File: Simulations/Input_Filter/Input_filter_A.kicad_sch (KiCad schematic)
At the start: 18 parts, among them U21 TL072

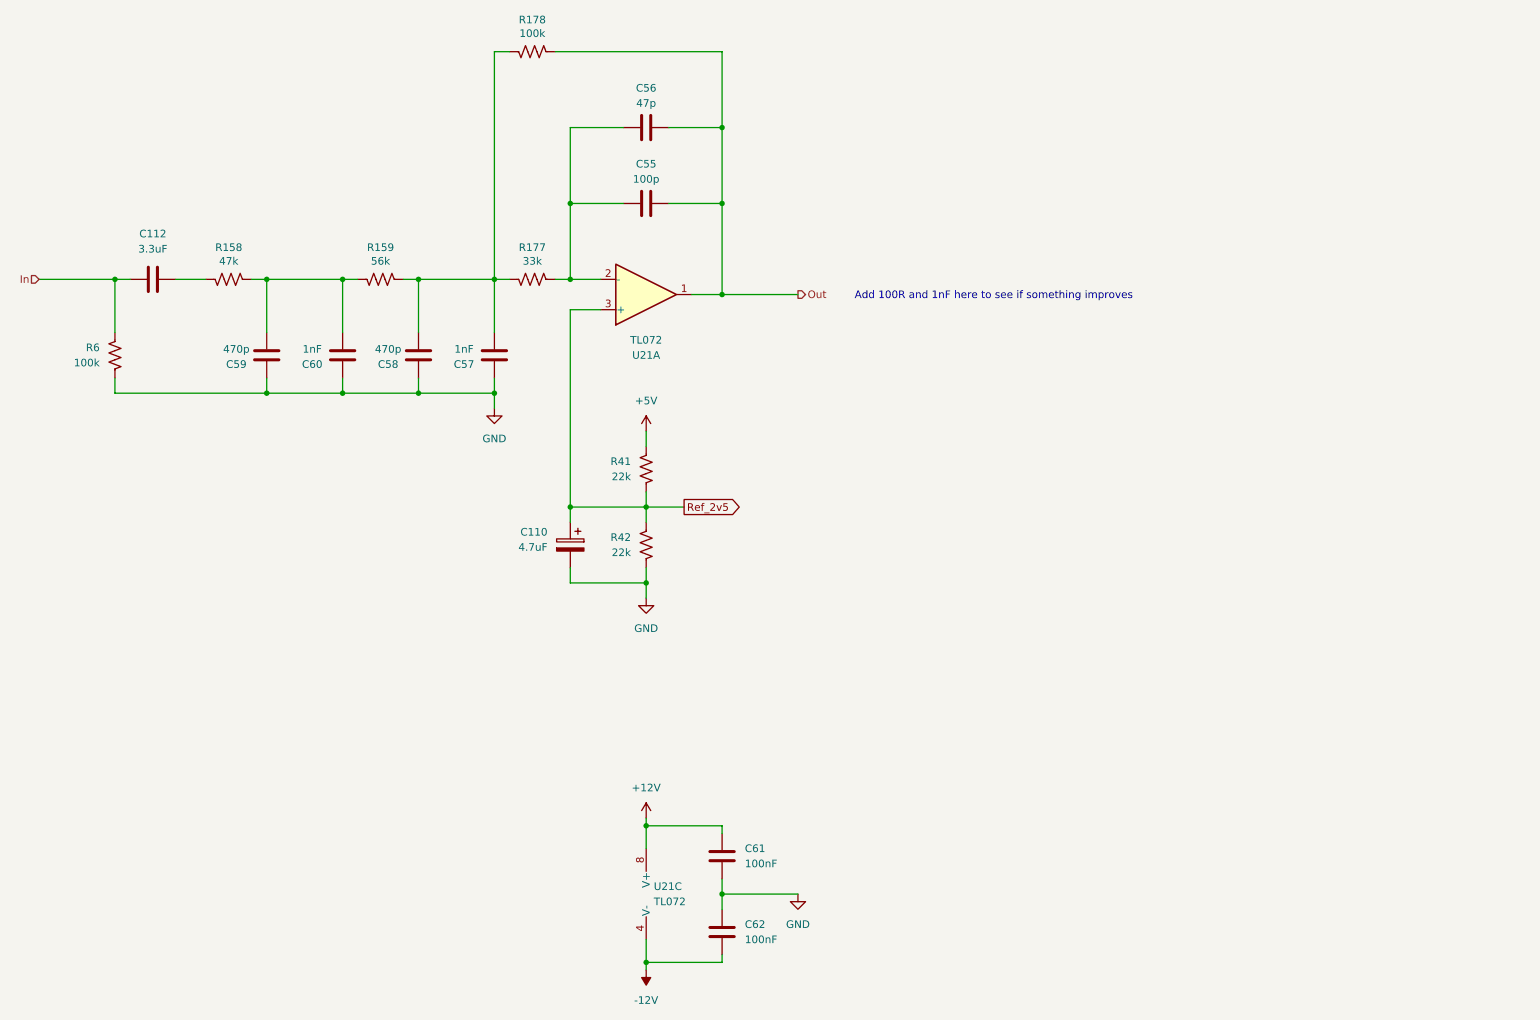
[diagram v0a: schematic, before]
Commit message: Simulated IO filters
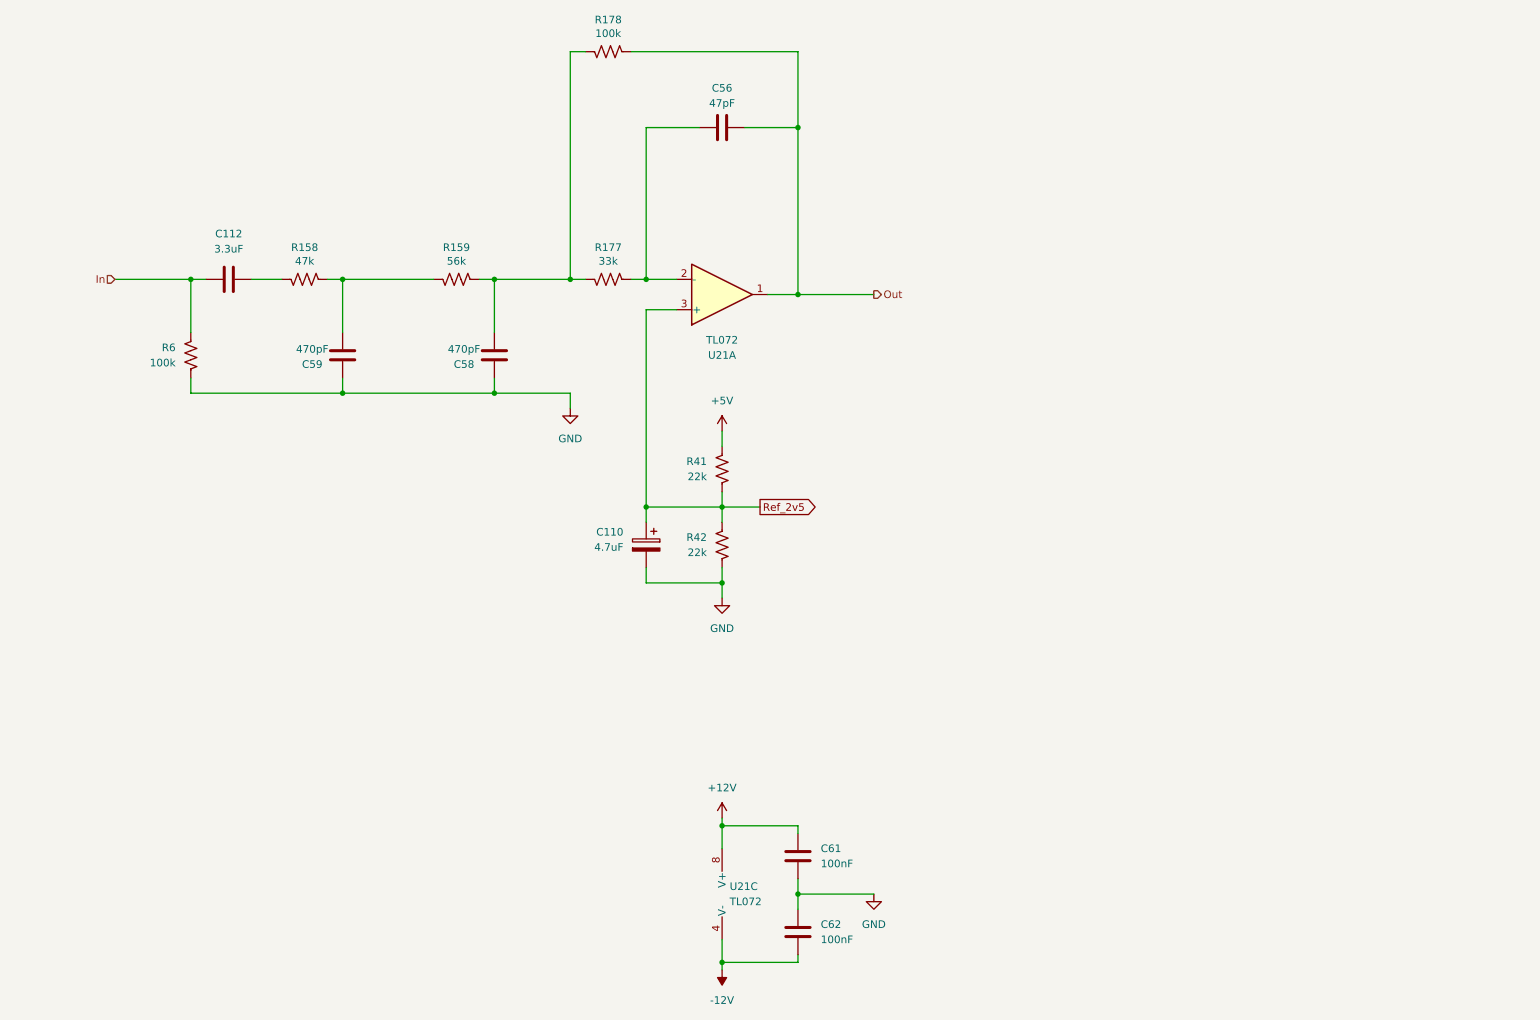
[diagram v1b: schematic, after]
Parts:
- removed C55: 100p, Capacitor_THT:C_Disc_D3.0mm_W2.0mm_P2.50mm, symbol Device:C
- removed C57, C60: 1nF, Capacitor_THT:C_Disc_D3.0mm_W2.0mm_P2.50mm, symbol Device:C
- C56: value 47p -> 47pF
- C58, C59: value 470p -> 470pF
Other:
- note removed: "Add 100R and 1nF here to see if something improves"
- company: DMH Instruments -> (none)

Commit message: Fixed issue with SPICE model
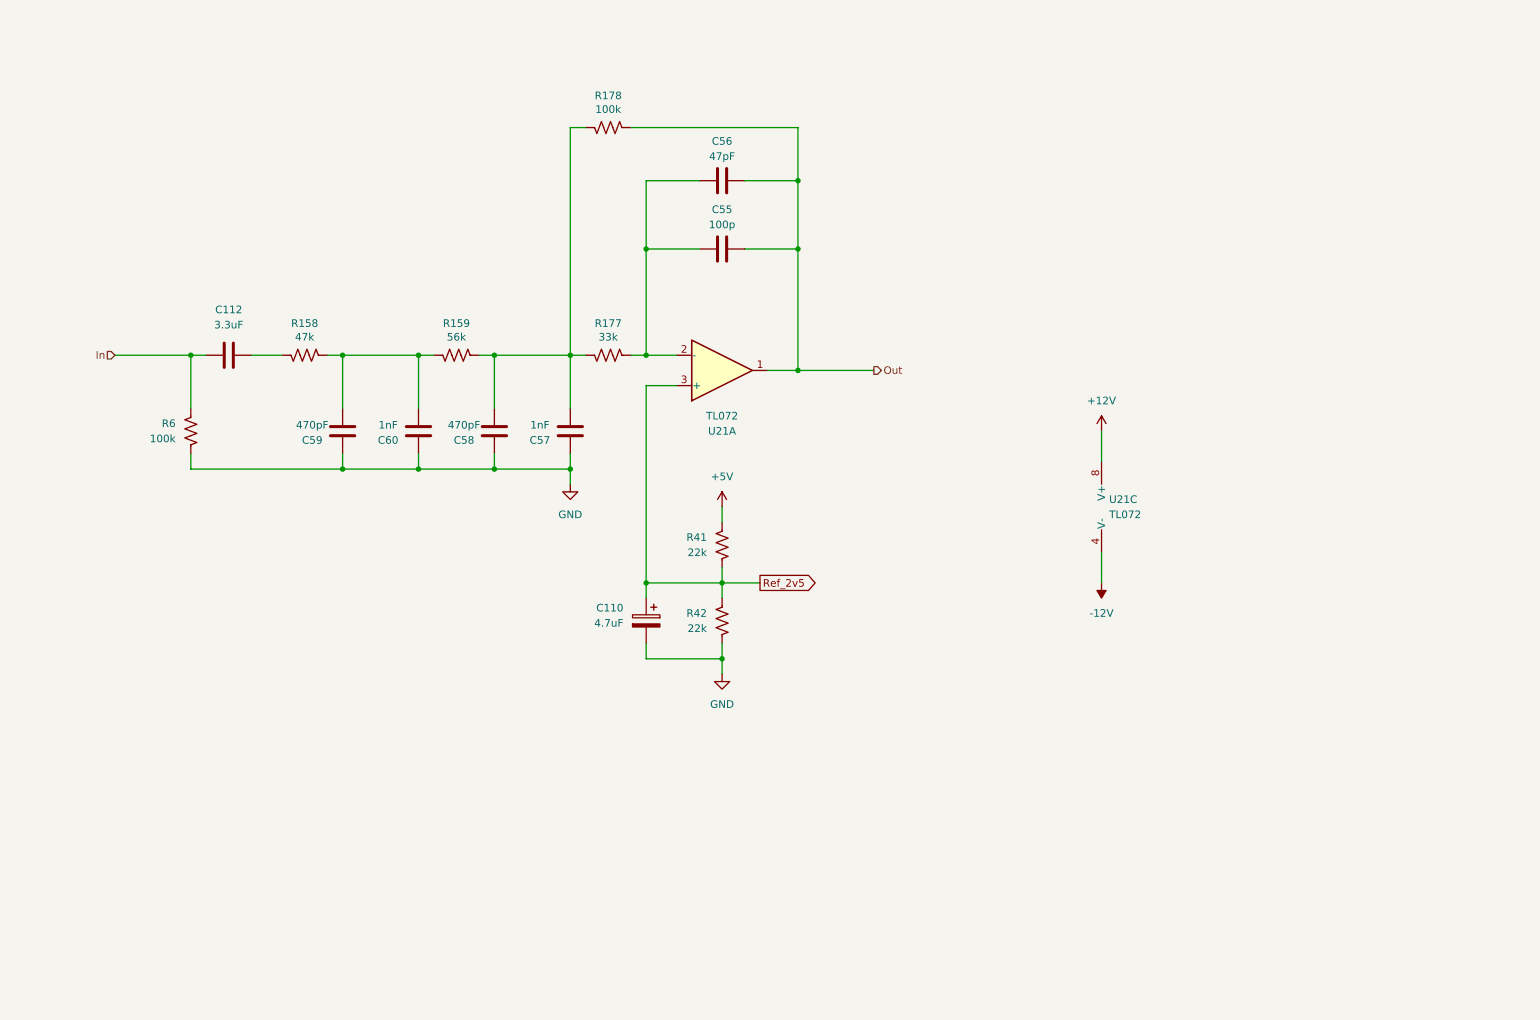
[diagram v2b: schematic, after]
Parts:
- removed C61, C62: 100nF, Capacitor_THT:C_Disc_D4.3mm_W1.9mm_P5.00mm, symbol Device:C
- added C55: 100p, Capacitor_THT:C_Disc_D3.0mm_W2.0mm_P2.50mm, symbol Device:C
- added C57, C60: 1nF, Capacitor_THT:C_Disc_D3.0mm_W2.0mm_P2.50mm, symbol Device:C
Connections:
- net GND: now also C57.1, C60.1
- net Out: now also C55.2
- net at C59.2, R158.2, R159.1: now also C60.2
- net at C58.2, R159.2, R177.1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: now also C57.2
- net at C56.1, R177.2, U21.2 (-): now also C55.1
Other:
- moved on the sheet: C110, C112, C56, C58, C59, R158, R159, R177, R178, R41, R42, R6

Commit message: Simulated clamping diodes inside filter
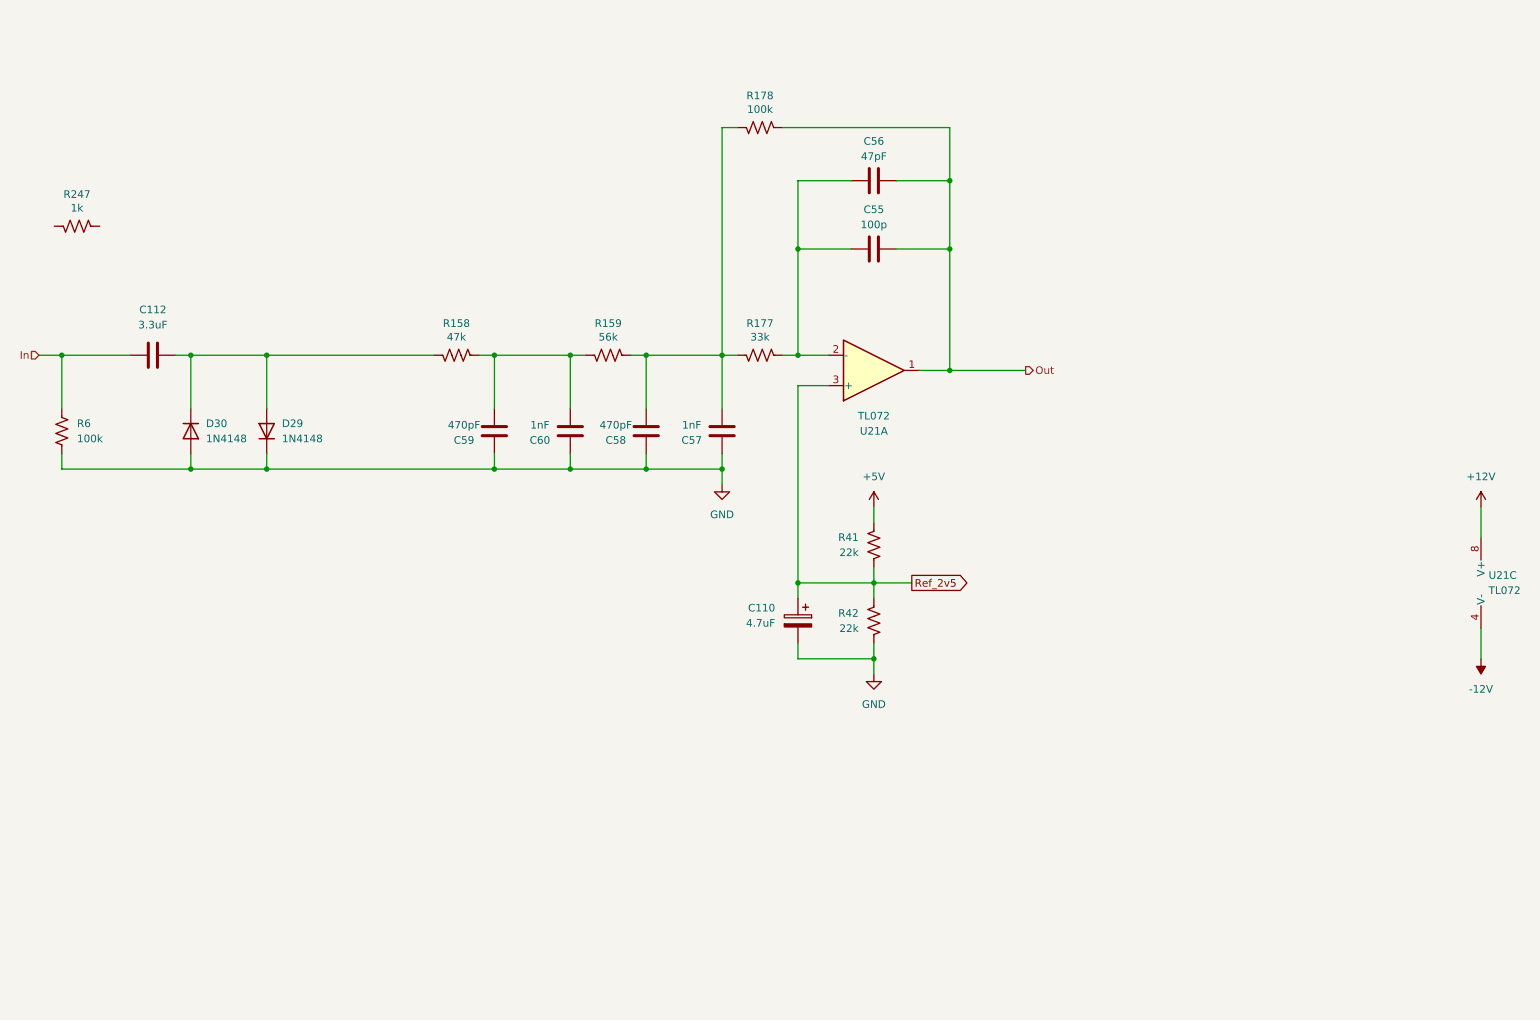
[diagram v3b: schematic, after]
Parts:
- added D29, D30: 1N4148, Diode_THT:D_DO-35_SOD27_P7.62mm_Horizontal, symbol Diode:1N4148
- added R247: 1k, Resistor_THT:R_Axial_DIN0207_L6.3mm_D2.5mm_P7.62mm_Horizontal, symbol Device:R_US
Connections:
- net GND: now also D29.1 (K), D30.2 (A)
- net at C112.2, R158.1: now also D29.2 (A), D30.1 (K)
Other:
- moved on the sheet: C110, C55, C56, C57, C58, C59, C60, R158, R159, R177, R178, R41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

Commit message: Synced channel A and B schematics
... and applied several minor improvements and optimizations.
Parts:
- C112: value 3.3uF -> 1uF
- C55: value 100p -> 150p
- C57, C60: value 1nF -> 1.5nF
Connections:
- net In: now also R247.1; no longer C112.1, R6.2
- net at C112.2, R158.1: no longer D29.2 (A), D30.1 (K)
- net at R247.2: now also C112.1, D29.2 (A), D30.1 (K), R6.2
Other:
- moved on the sheet: R247

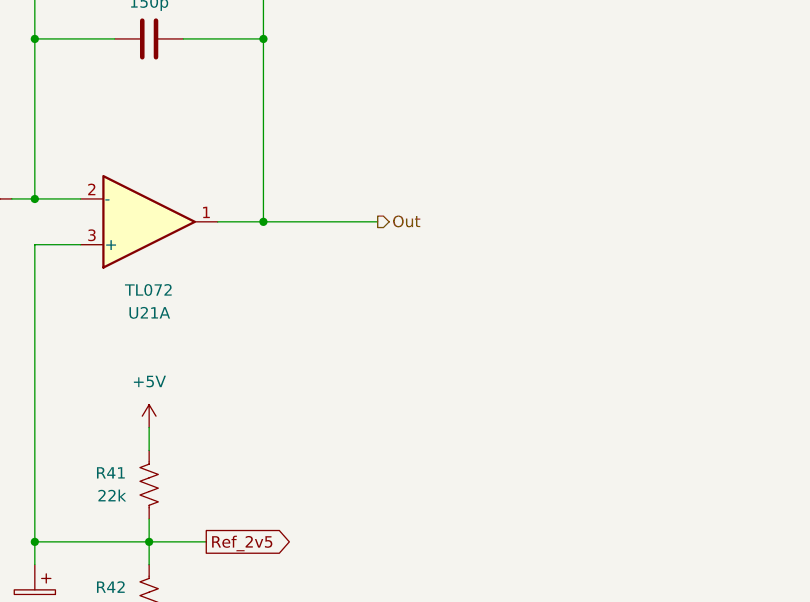
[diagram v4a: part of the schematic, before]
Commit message: Added anti-ringing RC network to IF sim
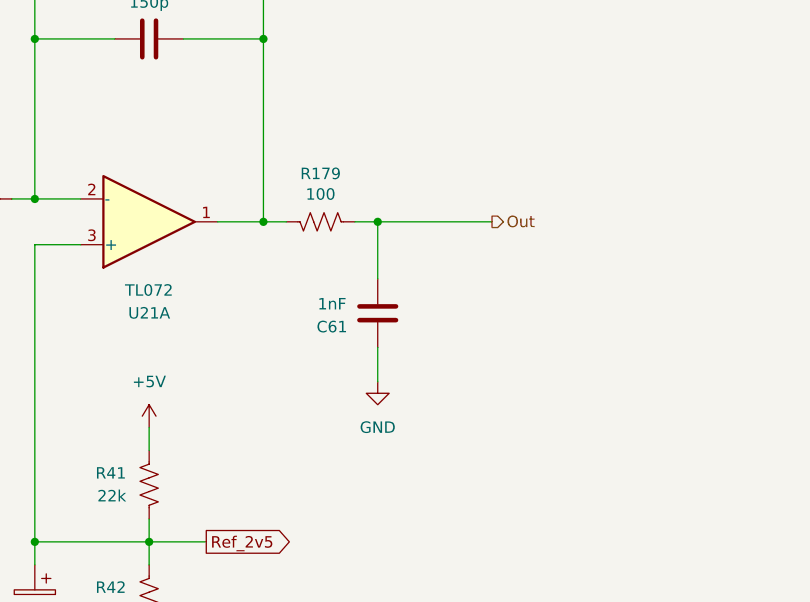
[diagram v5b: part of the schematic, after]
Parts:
- added C61: 1nF, Capacitor_THT:C_Disc_D3.0mm_W2.0mm_P2.50mm, symbol Device:C
- added R179: 100, Resistor_THT:R_Axial_DIN0207_L6.3mm_D2.5mm_P7.62mm_Horizontal, symbol Device:R_US
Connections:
- net GND: now also C61.1
- net Out: now also C61.2, R179.2; no longer C55.2, C56.2, R178.2, U21.1
- new net: C55.2, C56.2, R178.2, R179.1, U21.1
